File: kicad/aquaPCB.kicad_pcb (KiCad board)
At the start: 2 copper layers, 100 x 100 mm, 106 parts, among them J1 12V IN, J19 1-wire DS1820, J2 Raspberry Pi, J22 I2C 1, J23 I2C 2, J24 Display, J26 ADC #1 in 2, J27 ADC #1 in 3, J4 PWM 0, J5 GPIO 12, J6 GPIO 13, J7 PWM 1, J8 GPIO 16, J9 GPIO 26, Q1 AOD4184A, Q10 AOD4185, Q2 AOD4184A, Q3 AOD4184A, Q4 AOD4184A, Q5 AOD4184A, Q6 AOD4184A, U1 TPS54360B, U2 AMS1117-3.3, U3 74HCT244D, U5 ADS1115IDGSR

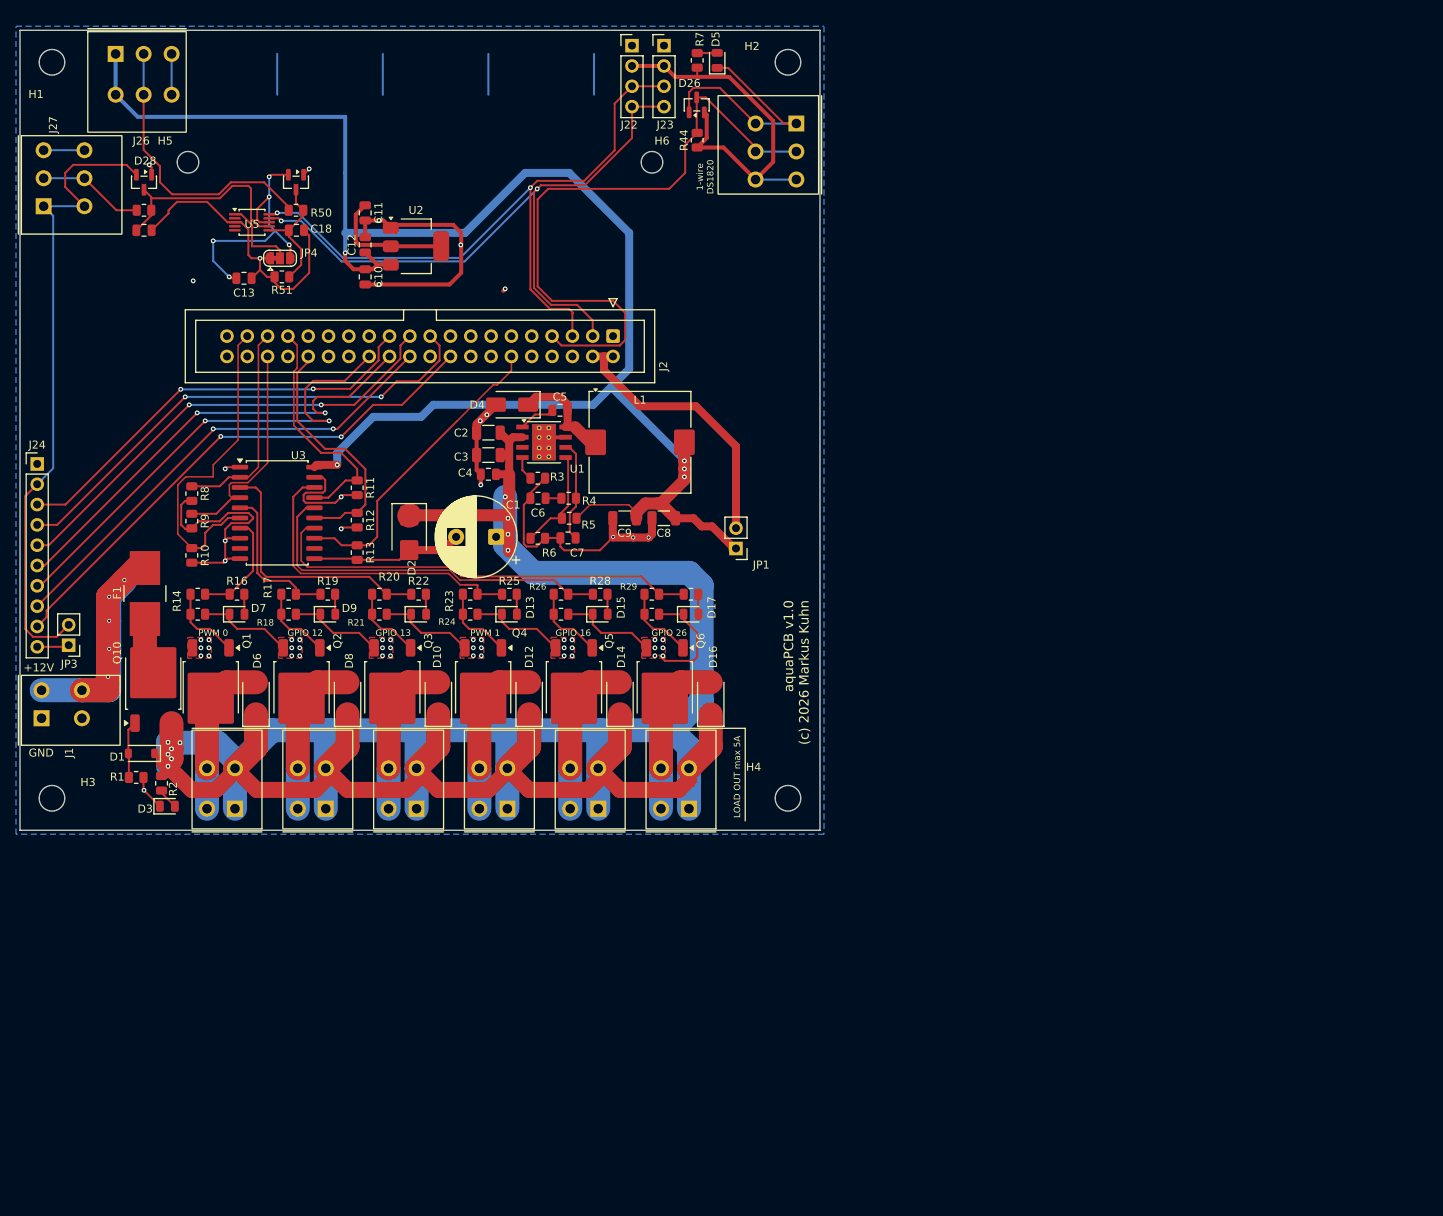
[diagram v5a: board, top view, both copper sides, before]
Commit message: kicad: v2 schematic and board update (PCA9685 x2, box-header ports, sensors, analog sockets)
New sheets pwm/powerbar/sensors; Q2/3/5/6 on PCA #1 ch 15-12; sensor GPIOs 5,6,20,21,22,23; 1-Wire +5V_EXT/Data/GND; four identical 0-5 V analog sockets; DC/LED/sensor ports as 2x4 box headers (pin n = Robo-Tank v3 RJ45 pin n). Board: 82 new footprints coarse-placed (56 parked beside the board), ERC 0, DRC copper 0, parity 0. README v2 plan updated.

Co-Authored-By: Claude Opus 5.5 <noreply@anthropic.com>
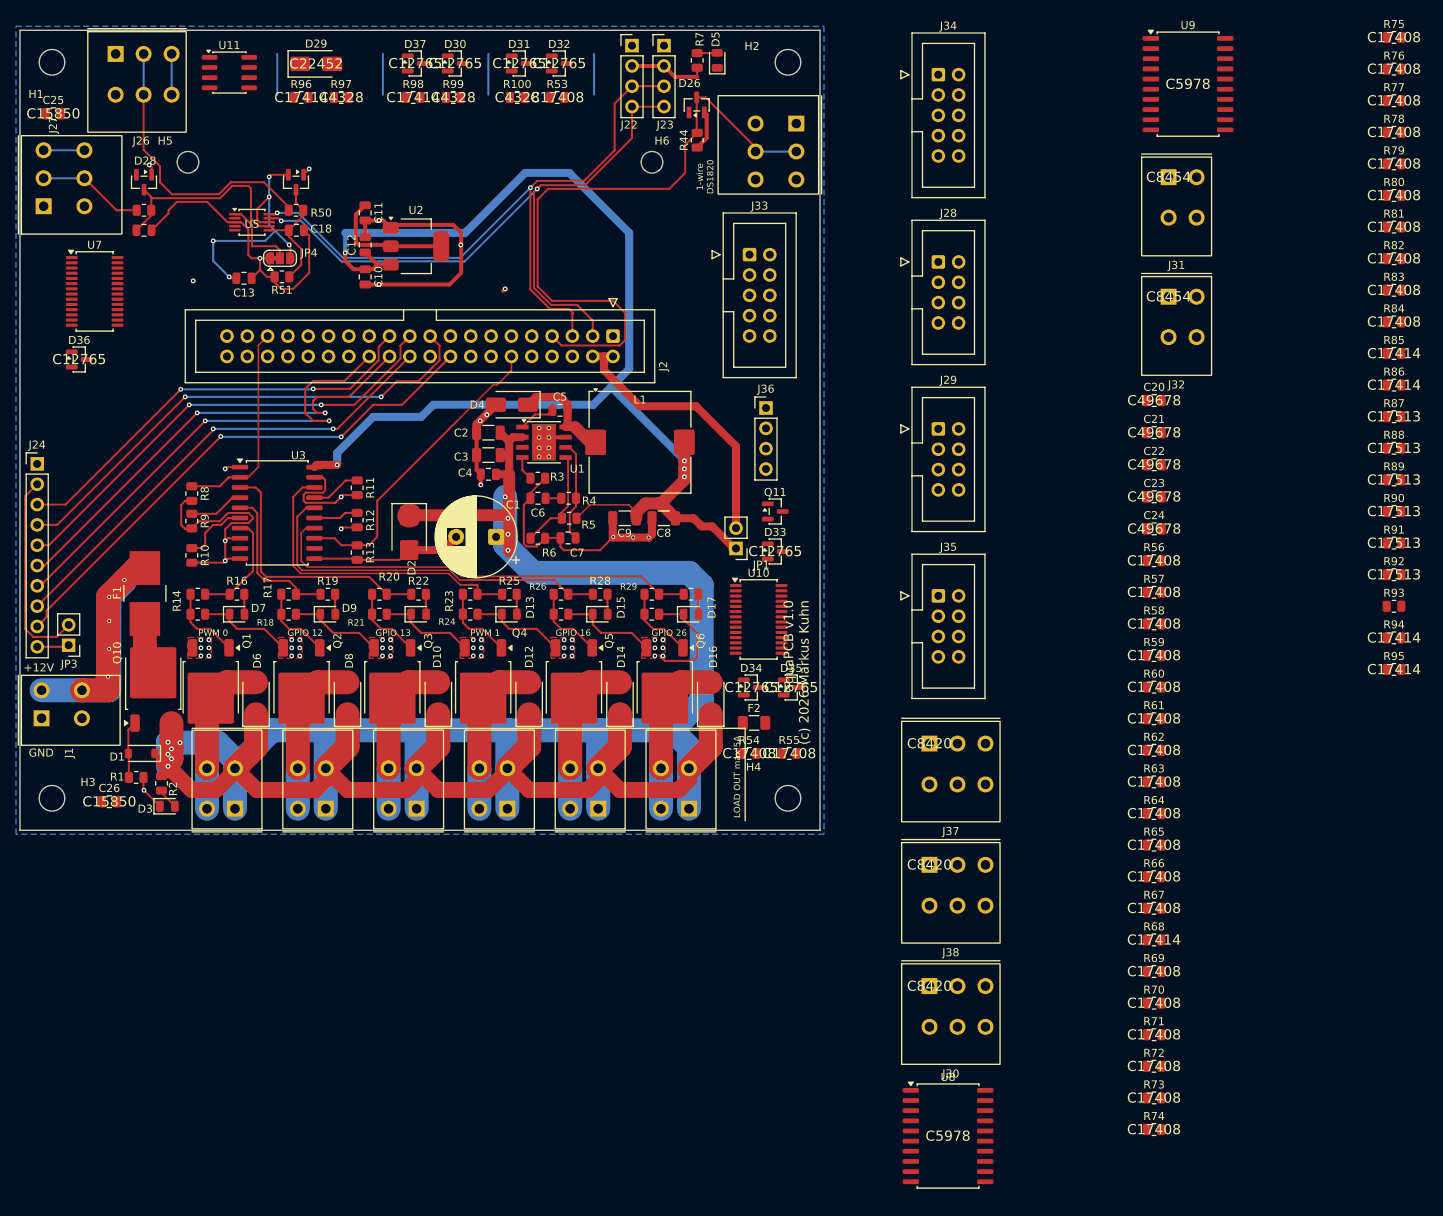
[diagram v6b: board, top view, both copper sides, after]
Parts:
- added C20: 100n, Capacitor_SMD:C_0805_2012Metric, F.Cu at (220.6, 82.0)
- added C21: 100n, Capacitor_SMD:C_0805_2012Metric, F.Cu at (220.6, 86.0)
- added C22: 100n, Capacitor_SMD:C_0805_2012Metric, F.Cu at (220.6, 90.0)
- added C23: 100n, Capacitor_SMD:C_0805_2012Metric, F.Cu at (220.6, 94.0)
- added C24: 100n, Capacitor_SMD:C_0805_2012Metric, F.Cu at (220.6, 98.0)
- added C25: 10u, Capacitor_SMD:C_0805_2012Metric, F.Cu at (83.0, 46.1)
- added C26: 10u, Capacitor_SMD:C_0805_2012Metric, F.Cu at (90.0, 132.1)
- added D29: SS54, Diode_SMD:D_SMA, F.Cu at (115.9, 39.9)
- added D30: BAT54S, Package_TO_SOT_SMD:SOT-23, F.Cu at (133.3, 39.8)
- added D31: BAT54S, Package_TO_SOT_SMD:SOT-23, F.Cu at (141.3, 39.8)
- added D32: BAT54S, Package_TO_SOT_SMD:SOT-23, F.Cu at (146.3, 39.8)
- added D33: BAT54S, Package_TO_SOT_SMD:SOT-23, F.Cu at (173.3, 100.8)
- added D34: BAT54S, Package_TO_SOT_SMD:SOT-23, F.Cu at (170.3, 117.8)
- added D35: BAT54S, Package_TO_SOT_SMD:SOT-23, F.Cu at (175.3, 117.8)
- added D36: BAT54S, Package_TO_SOT_SMD:SOT-23, F.Cu at (86.3, 76.8)
- added D37: BAT54S, Package_TO_SOT_SMD:SOT-23, F.Cu at (128.3, 39.8)
- added F2: PTC 0.5A, Fuse:Fuse_1206_3216Metric, F.Cu at (170.6, 122.3)
- added J28: DC ports, Connector_IDC:IDC-Header_2x04_P2.54mm_Vertical, F.Cu at (193.6, 64.6)
- added J29: LED ports, Connector_IDC:IDC-Header_2x04_P2.54mm_Vertical, F.Cu at (193.6, 85.5)
- added J30: PCA9685 #1 ch 0, aquaPCB:TerminalBlock_Kangnex_WJ250B-3.5-03P_P3.50mm_Staggered, F.Cu at (192.5, 155.2)
- added J31: Float 1, aquaPCB:TerminalBlock_Kangnex_WJ250B-3.5-02P_P3.50mm_Staggered, F.Cu at (222.4, 54.0)
- added J32: Float 2, aquaPCB:TerminalBlock_Kangnex_WJ250B-3.5-02P_P3.50mm_Staggered, F.Cu at (222.4, 69.0)
- added J33: Power bar 1, Connector_IDC:IDC-Header_2x05_P2.54mm_Vertical, F.Cu at (170.0, 63.7)
- added J34: Power bar 2, Connector_IDC:IDC-Header_2x05_P2.54mm_Vertical, F.Cu at (193.6, 41.2)
- added J35: Sensors, Connector_IDC:IDC-Header_2x04_P2.54mm_Vertical, F.Cu at (193.6, 106.4)
- added J36: I2C 5V, Connector_PinHeader_2.54mm:PinHeader_1x04_P2.54mm_Vertical, F.Cu at (172.1, 82.9)
- added J37: ADC #1 in 0, aquaPCB:TerminalBlock_Kangnex_WJ250B-3.5-03P_P3.50mm_Staggered, F.Cu at (192.5, 124.8)
- added J38: ADC #1 in 1, aquaPCB:TerminalBlock_Kangnex_WJ250B-3.5-03P_P3.50mm_Staggered, F.Cu at (192.5, 140.0)
- added Q11: AO3400A, Package_TO_SOT_SMD:SOT-23, F.Cu at (173.3, 95.8)
- added R100: 20k, Resistor_SMD:R_0805_2012Metric, F.Cu at (141.0, 44.1)
- added R53: 100, Resistor_SMD:R_0805_2012Metric, F.Cu at (146.0, 44.1)
- added R54: 100, Resistor_SMD:R_0805_2012Metric, F.Cu at (170.0, 126.1)
- added R55: 100, Resistor_SMD:R_0805_2012Metric, F.Cu at (175.0, 126.1)
- added R56: 100, Resistor_SMD:R_0805_2012Metric, F.Cu at (220.6, 102.0)
- added R57: 100, Resistor_SMD:R_0805_2012Metric, F.Cu at (220.6, 105.9)
- added R58: 100, Resistor_SMD:R_0805_2012Metric, F.Cu at (220.6, 109.9)
- added R59: 100, Resistor_SMD:R_0805_2012Metric, F.Cu at (220.6, 113.8)
- added R60: 100, Resistor_SMD:R_0805_2012Metric, F.Cu at (220.6, 117.8)
- added R61: 100, Resistor_SMD:R_0805_2012Metric, F.Cu at (220.6, 121.7)
- added R62: 100, Resistor_SMD:R_0805_2012Metric, F.Cu at (220.6, 125.7)
- added R63: 100, Resistor_SMD:R_0805_2012Metric, F.Cu at (220.6, 129.6)
- added R64: 100, Resistor_SMD:R_0805_2012Metric, F.Cu at (220.6, 133.6)
- added R65: 100, Resistor_SMD:R_0805_2012Metric, F.Cu at (220.6, 137.5)
- added R66: 100, Resistor_SMD:R_0805_2012Metric, F.Cu at (220.6, 141.5)
- added R67: 100, Resistor_SMD:R_0805_2012Metric, F.Cu at (220.6, 145.4)
- added R68: 10k, Resistor_SMD:R_0805_2012Metric, F.Cu at (220.6, 149.4)
- added R69: 100, Resistor_SMD:R_0805_2012Metric, F.Cu at (220.6, 153.3)
- added R70: 100, Resistor_SMD:R_0805_2012Metric, F.Cu at (220.6, 157.3)
- added R71: 100, Resistor_SMD:R_0805_2012Metric, F.Cu at (220.6, 161.2)
- added R72: 100, Resistor_SMD:R_0805_2012Metric, F.Cu at (220.6, 165.2)
- added R73: 100, Resistor_SMD:R_0805_2012Metric, F.Cu at (220.6, 169.1)
- added R74: 100, Resistor_SMD:R_0805_2012Metric, F.Cu at (220.6, 173.1)
- added R75: 100, Resistor_SMD:R_0805_2012Metric, F.Cu at (250.6, 36.6)
- added R76: 100, Resistor_SMD:R_0805_2012Metric, F.Cu at (250.6, 40.5)
- added R77: 100, Resistor_SMD:R_0805_2012Metric, F.Cu at (250.6, 44.5)
- added R78: 100, Resistor_SMD:R_0805_2012Metric, F.Cu at (250.6, 48.4)
- added R79: 100, Resistor_SMD:R_0805_2012Metric, F.Cu at (250.6, 52.4)
- added R80: 100, Resistor_SMD:R_0805_2012Metric, F.Cu at (250.6, 56.3)
- added R81: 100, Resistor_SMD:R_0805_2012Metric, F.Cu at (250.6, 60.3)
- added R82: 100, Resistor_SMD:R_0805_2012Metric, F.Cu at (250.6, 64.2)
- added R83: 100, Resistor_SMD:R_0805_2012Metric, F.Cu at (250.6, 68.2)
- added R84: 100, Resistor_SMD:R_0805_2012Metric, F.Cu at (250.6, 72.1)
- added R85: 10k, Resistor_SMD:R_0805_2012Metric, F.Cu at (250.6, 76.1)
- added R86: 10k, Resistor_SMD:R_0805_2012Metric, F.Cu at (250.6, 80.0)
- added R87: 1k, Resistor_SMD:R_0805_2012Metric, F.Cu at (250.6, 84.0)
- added R88: 1k, Resistor_SMD:R_0805_2012Metric, F.Cu at (250.6, 87.9)
- added R89: 1k, Resistor_SMD:R_0805_2012Metric, F.Cu at (250.6, 91.9)
- added R90: 1k, Resistor_SMD:R_0805_2012Metric, F.Cu at (250.6, 95.8)
- added R91: 1k, Resistor_SMD:R_0805_2012Metric, F.Cu at (250.6, 99.8)
- added R92: 1k, Resistor_SMD:R_0805_2012Metric, F.Cu at (250.6, 103.7)
- added R93: 200k, Resistor_SMD:R_0805_2012Metric, F.Cu at (250.6, 107.7)
- added R94: 10k, Resistor_SMD:R_0805_2012Metric, F.Cu at (250.6, 111.6)
- added R95: 10k, Resistor_SMD:R_0805_2012Metric, F.Cu at (250.6, 115.6)
- added R96: 10k, Resistor_SMD:R_0805_2012Metric, F.Cu at (114.0, 44.1)
- added R97: 20k, Resistor_SMD:R_0805_2012Metric, F.Cu at (119.0, 44.1)
- added R98: 10k, Resistor_SMD:R_0805_2012Metric, F.Cu at (128.0, 44.1)
- added R99: 20k, Resistor_SMD:R_0805_2012Metric, F.Cu at (133.0, 44.1)
- added U10: PCA9685PW, Package_SO:TSSOP-28_4.4x9.7mm_P0.65mm, F.Cu at (171.2, 109.3)
- added U11: PCA9306D, Package_SO:SOIC-8_3.9x4.9mm_P1.27mm, F.Cu at (105.0, 41.0)
- added U7: PCA9685PW, Package_SO:TSSOP-28_4.4x9.7mm_P0.65mm, F.Cu at (88.2, 68.3)
- added U8: 74HCT244D, Package_SO:SOIC-20W_7.5x12.8mm_P1.27mm, F.Cu at (194.9, 173.9)
- added U9: 74HCT244D, Package_SO:SOIC-20W_7.5x12.8mm_P1.27mm, F.Cu at (224.9, 42.4)
- C19: value 100n -> 10u
- R52: value 1k -> 10k
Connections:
- net /ADS1115 ADC and pH amplifier/AIN2 renamed /ADS1115 ADC and analog sockets/AIN2
- net /ADS1115 ADC and pH amplifier/AIN3 renamed /ADS1115 ADC and analog sockets/AIN3
- J19 pad 1: GND -> +5V_EXT
- J19 pad 3: +3V3 -> GND
- J2 pad 15: unconnected-(J2-Pin_15-Pad15) -> GPIO22_SENS5
- J2 pad 16: unconnected-(J2-Pin_16-Pad16) -> GPIO23_SENS6
- J2 pad 29: unconnected-(J2-Pin_29-Pad29) -> GPIO5_SENS1
- J2 pad 31: unconnected-(J2-Pin_31-Pad31) -> GPIO6_SENS2
- J2 pad 32: GPIO12_Q2 -> unconnected-(J2-Pin_32-Pad32)
- J2 pad 33: GPIO13_Q3 -> unconnected-(J2-Pin_33-Pad33)
- J2 pad 36: GPIO16_Q5 -> unconnected-(J2-Pin_36-Pad36)
- J2 pad 37: GPIO26_Q6 -> unconnected-(J2-Pin_37-Pad37)
- J2 pad 38: unconnected-(J2-Pin_38-Pad38) -> GPIO20_SENS3
- J2 pad 40: unconnected-(J2-Pin_40-Pad40) -> GPIO21_SENS4
- J26 pad 1: +5V -> +5V_EXT
- J27 pad 1: +3V3 -> +5V_EXT
- R10 pad 1: GPIO26_Q6 -> PCA1_CH12
- R11 pad 1: GPIO13_Q3 -> PCA1_CH14
- R12 pad 1: GPIO12_Q2 -> PCA1_CH15
- R9 pad 1: GPIO16_Q5 -> PCA1_CH13
- U3 pad 15: GPIO12_Q2 -> PCA1_CH15
- U3 pad 17: GPIO13_Q3 -> PCA1_CH14
- U3 pad 4: GPIO16_Q5 -> PCA1_CH13
- U3 pad 6: GPIO26_Q6 -> PCA1_CH12
- U5 pad 4: unconnected-(U5-AIN0-Pad4) -> /ADS1115 ADC and analog sockets/AIN0
- U5 pad 5: unconnected-(U5-AIN1-Pad5) -> /ADS1115 ADC and analog sockets/AIN1
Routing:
- net +3V3: track 179.9 -> 89.7 mm
- net +5V: track 214.0 -> 164.5 mm
- net GPIO26_Q6: track 41.3 -> 0.00 mm
- net GPIO13_Q3: track 31.3 -> 0.00 mm
- net GPIO12_Q2: track 31.2 -> 0.00 mm
- net GND: track 327.2 -> 296.4 mm
- net GPIO16_Q5: track 28.8 -> 0.00 mm
- net PCA1_CH12: track 0.00 -> 8.44 mm
- net PCA1_CH13: track 0.00 -> 7.89 mm
- net PCA1_CH14: track 0.00 -> 6.24 mm
- net PCA1_CH15: track 0.00 -> 5.61 mm
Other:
- board text removed: "+3V3"
